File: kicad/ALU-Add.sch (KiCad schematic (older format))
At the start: 12 parts, among them U81 74LS245, U82 74LS283, U83 74LS283, U84 74LS86, U85 74LS86, U86 74LS86, U87 74LS86, U88 74LS86, U89 74LS86, U90 74LS86, U91 74LS86, U92 74LS86

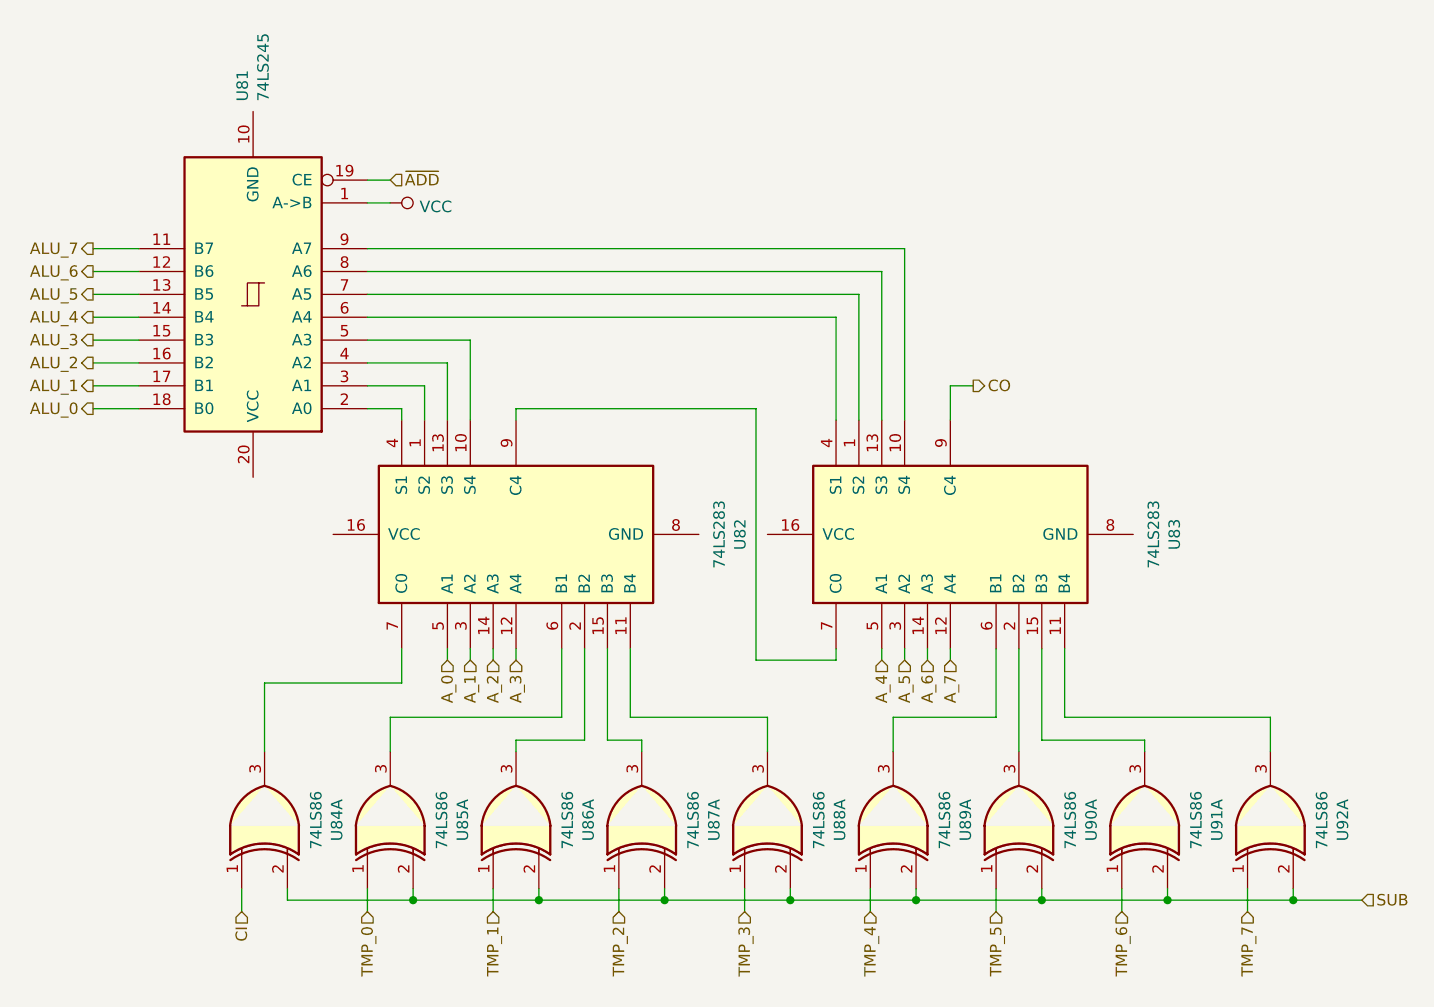
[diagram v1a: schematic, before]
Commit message: Reorganize part references
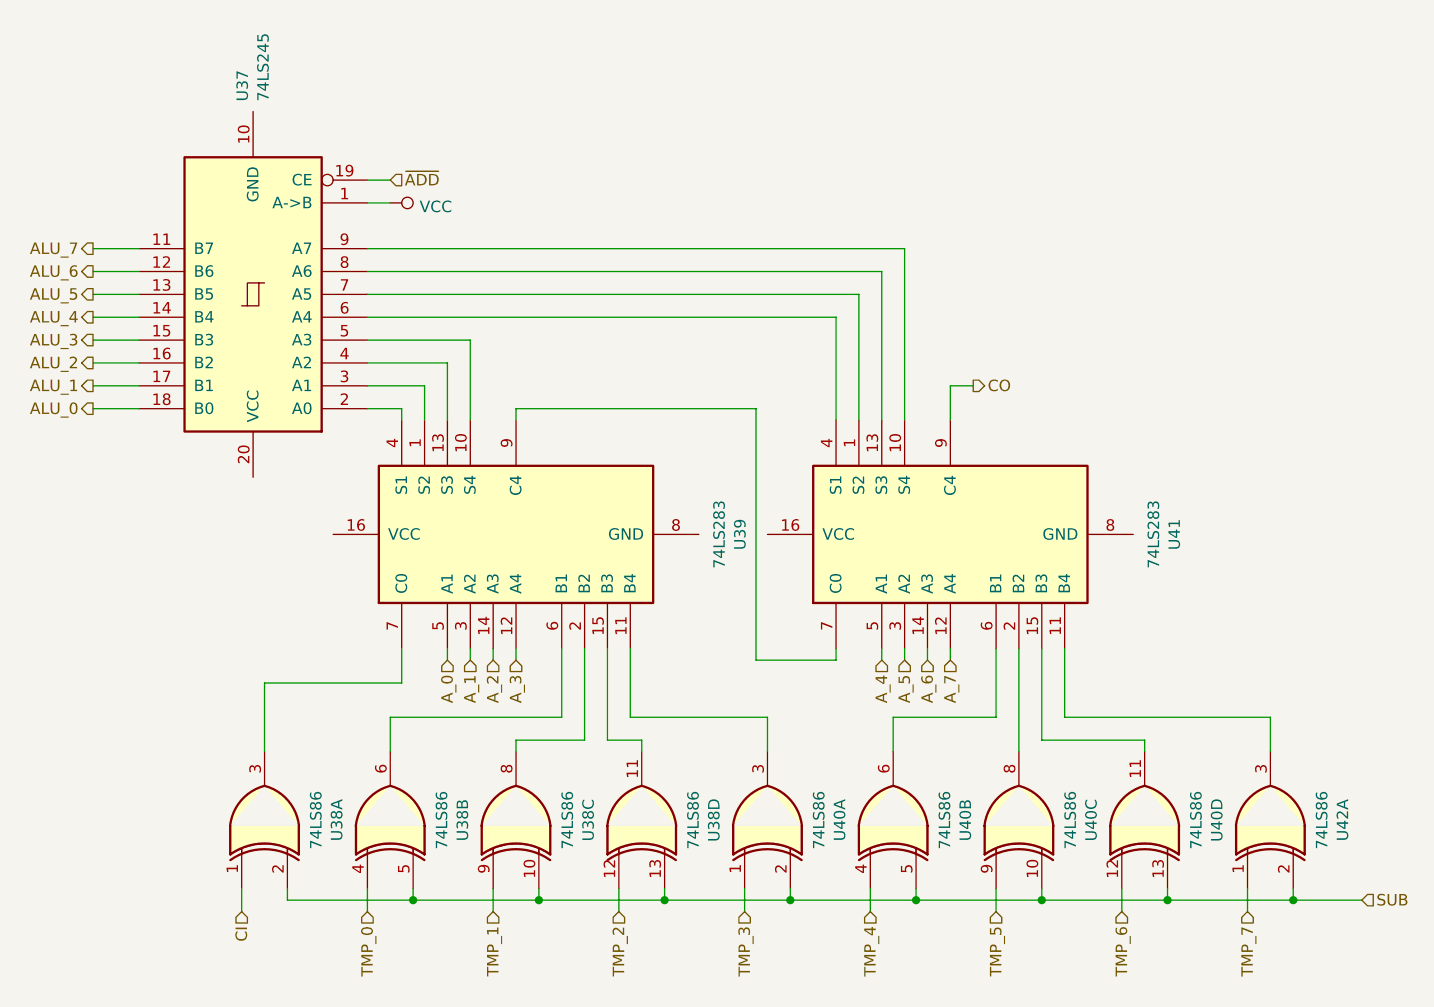
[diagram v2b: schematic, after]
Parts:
- renumbered U81 to U37, U84 to U38, U86 to U38, U85 to U38, U87 to U38, U82 to U39, U88 to U40, U90 to U40, U89 to U40, U91 to U40, U83 to U41, U92 to U42
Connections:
- net SUB: now also U38.10, U38.13, U38.5, U40.10, U40.13, U40.5; no longer U38.2, U38.2, U38.2, U40.2, U40.2, U40.2
- net TMP_0: now also U38.4; no longer U38.1
- net TMP_1: now also U38.9; no longer U38.1
- net TMP_2: now also U38.12; no longer U38.1
- net TMP_4: now also U40.4; no longer U40.1
- net TMP_5: now also U40.9; no longer U40.1
- net TMP_6: now also U40.12; no longer U40.1
- net at U39.2 (B2): now also U38.8; no longer U38.3
- net at U39.6 (B1): now also U38.6; no longer U38.3
- net at U39.15 (B3): now also U38.11; no longer U38.3
- net at U41.2 (B2): now also U40.8; no longer U40.3
- net at U41.6 (B1): now also U40.6; no longer U40.3
- net at U41.15 (B3): now also U40.11; no longer U40.3
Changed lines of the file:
@@
 $Descr A4 11693 8268
 encoding utf-8
-Sheet 23 26
+Sheet 10 26
 Title ""
 Date "2019-10-03"
@@
 AR Path="/5E5B2E62/5D96F636" Ref="U?"  Part="1"
 AR Path="/5E5B2E62/5E0141CE/5D96F636" Ref="U?"  Part="1"
-AR Path="/5E5B2E62/5E0141CE/5D94D587/5D96F636" Ref="U84"  Part="1"
-F 0 "U84" H 3200 4933 50  0000 C CNN
+AR Path="/5E5B2E62/5E0141CE/5D94D587/5D96F636" Ref="U38"  Part="1"
+F 0 "U38" H 3200 4933 50  0000 C CNN
 F 1 "74LS86" H 3200 5024 50  0000 C CNN
 F 2 "" H 3200 5250 50  0001 C CNN
@@
 $Comp
 L 74xx:74LS86 U?
-U 1 1 5D96F66E
+U 3 1 5D96F66E
 P 4300 5250
 AR Path="/5E5B2E62/5D96F66E" Ref="U?"  Part="1"
 AR Path="/5E5B2E62/5E0141CE/5D96F66E" Ref="U?"  Part="1"
-AR Path="/5E5B2E62/5E0141CE/5D94D587/5D96F66E" Ref="U86"  Part="1"
-F 0 "U86" H 4300 4933 50  0000 C CNN
+AR Path="/5E5B2E62/5E0141CE/5D94D587/5D96F66E" Ref="U38"  Part="3"
+F 0 "U38" H 4300 4933 50  0000 C CNN
 F 1 "74LS86" H 4300 5024 50  0000 C CNN
 F 2 "" H 4300 5250 50  0001 C CNN
 F 3 "74xx/74ls86.pdf" H 4300 5250 50  0001 C CNN
-	1    4300 5250
-	0    -1   -1   0
-$EndComp
-$Comp
-L 74xx:74LS86 U?
-U 1 1 5D96F674
+	3    4300 5250
+	0    -1   -1   0
+$EndComp
+$Comp
+L 74xx:74LS86 U?
+U 2 1 5D96F674
 P 3750 5250
 AR Path="/5E5B2E62/5D96F674" Ref="U?"  Part="1"
 AR Path="/5E5B2E62/5E0141CE/5D96F674" Ref="U?"  Part="1"
-AR Path="/5E5B2E62/5E0141CE/5D94D587/5D96F674" Ref="U85"  Part="1"
-F 0 "U85" H 3750 4933 50  0000 C CNN
+AR Path="/5E5B2E62/5E0141CE/5D94D587/5D96F674" Ref="U38"  Part="2"
+F 0 "U38" H 3750 4933 50  0000 C CNN
 F 1 "74LS86" H 3750 5024 50  0000 C CNN
 F 2 "" H 3750 5250 50  0001 C CNN
 F 3 "74xx/74ls86.pdf" H 3750 5250 50  0001 C CNN
-	1    3750 5250
+	2    3750 5250
 	0    -1   -1   0
 $EndComp
@@
 AR Path="/5E5B2E62/5D96F67A" Ref="U?"  Part="1"
 AR Path="/5E5B2E62/5E0141CE/5D96F67A" Ref="U?"  Part="1"
-AR Path="/5E5B2E62/5E0141CE/5D94D587/5D96F67A" Ref="U88"  Part="1"
-F 0 "U88" H 5400 4933 50  0000 C CNN
+AR Path="/5E5B2E62/5E0141CE/5D94D587/5D96F67A" Ref="U40"  Part="1"
+F 0 "U40" H 5400 4933 50  0000 C CNN
 F 1 "74LS86" H 5400 5024 50  0000 C CNN
 F 2 "" H 5400 5250 50  0001 C CNN
@@
 $Comp
 L 74xx:74LS86 U?
-U 1 1 5D96F680
+U 4 1 5D96F680
 P 4850 5250
 AR Path="/5E5B2E62/5D96F680" Ref="U?"  Part="1"
 AR Path="/5E5B2E62/5E0141CE/5D96F680" Ref="U?"  Part="1"
-AR Path="/5E5B2E62/5E0141CE/5D94D587/5D96F680" Ref="U87"  Part="1"
-F 0 "U87" H 4850 4933 50  0000 C CNN
+AR Path="/5E5B2E62/5E0141CE/5D94D587/5D96F680" Ref="U38"  Part="4"
+F 0 "U38" H 4850 4933 50  0000 C CNN
 F 1 "74LS86" H 4850 5024 50  0000 C CNN
 F 2 "" H 4850 5250 50  0001 C CNN
 F 3 "74xx/74ls86.pdf" H 4850 5250 50  0001 C CNN
-	1    4850 5250
+	4    4850 5250
 	0    -1   -1   0
 $EndComp
@@
 $Comp
 L 74xx:74LS86 U?
-U 1 1 5D96F68F
+U 3 1 5D96F68F
 P 6500 5250
 AR Path="/5E5B2E62/5D96F68F" Ref="U?"  Part="1"
 AR Path="/5E5B2E62/5E0141CE/5D96F68F" Ref="U?"  Part="1"
-AR Path="/5E5B2E62/5E0141CE/5D94D587/5D96F68F" Ref="U90"  Part="1"
-F 0 "U90" H 6500 4933 50  0000 C CNN
+AR Path="/5E5B2E62/5E0141CE/5D94D587/5D96F68F" Ref="U40"  Part="3"
+F 0 "U40" H 6500 4933 50  0000 C CNN
 F 1 "74LS86" H 6500 5024 50  0000 C CNN
 F 2 "" H 6500 5250 50  0001 C CNN
 F 3 "74xx/74ls86.pdf" H 6500 5250 50  0001 C CNN
-	1    6500 5250
-	0    -1   -1   0
-$EndComp
-$Comp
-L 74xx:74LS86 U?
-U 1 1 5D96F695
+	3    6500 5250
+	0    -1   -1   0
+$EndComp
+$Comp
+L 74xx:74LS86 U?
+U 2 1 5D96F695
 P 5950 5250
 AR Path="/5E5B2E62/5D96F695" Ref="U?"  Part="1"
 AR Path="/5E5B2E62/5E0141CE/5D96F695" Ref="U?"  Part="1"
-AR Path="/5E5B2E62/5E0141CE/5D94D587/5D96F695" Ref="U89"  Part="1"
-F 0 "U89" H 5950 4933 50  0000 C CNN
+AR Path="/5E5B2E62/5E0141CE/5D94D587/5D96F695" Ref="U40"  Part="2"
+F 0 "U40" H 5950 4933 50  0000 C CNN
 F 1 "74LS86" H 5950 5024 50  0000 C CNN
 F 2 "" H 5950 5250 50  0001 C CNN
 F 3 "74xx/74ls86.pdf" H 5950 5250 50  0001 C CNN
-	1    5950 5250
+	2    5950 5250
 	0    -1   -1   0
 $EndComp
@@
 AR Path="/5E5B2E62/5D96F69B" Ref="U?"  Part="1"
 AR Path="/5E5B2E62/5E0141CE/5D96F69B" Ref="U?"  Part="1"
-AR Path="/5E5B2E62/5E0141CE/5D94D587/5D96F69B" Ref="U92"  Part="1"
-F 0 "U92" H 7600 4933 50  0000 C CNN
+AR Path="/5E5B2E62/5E0141CE/5D94D587/5D96F69B" Ref="U42"  Part="1"
+F 0 "U42" H 7600 4933 50  0000 C CNN
 F 1 "74LS86" H 7600 5024 50  0000 C CNN
 F 2 "" H 7600 5250 50  0001 C CNN
@@
 $Comp
 L 74xx:74LS86 U?
-U 1 1 5D96F6A1
+U 4 1 5D96F6A1
 P 7050 5250
 AR Path="/5E5B2E62/5D96F6A1" Ref="U?"  Part="1"
 AR Path="/5E5B2E62/5E0141CE/5D96F6A1" Ref="U?"  Part="1"
-AR Path="/5E5B2E62/5E0141CE/5D94D587/5D96F6A1" Ref="U91"  Part="1"
-F 0 "U91" H 7050 4933 50  0000 C CNN
+AR Path="/5E5B2E62/5E0141CE/5D94D587/5D96F6A1" Ref="U40"  Part="4"
+F 0 "U40" H 7050 4933 50  0000 C CNN
 F 1 "74LS86" H 7050 5024 50  0000 C CNN
 F 2 "" H 7050 5250 50  0001 C CNN
 F 3 "74xx/74ls86.pdf" H 7050 5250 50  0001 C CNN
-	1    7050 5250
+	4    7050 5250
 	0    -1   -1   0
 $EndComp
@@
 AR Path="/5E5B2E62/5D96F6BB" Ref="U?"  Part="1"
 AR Path="/5E5B2E62/5E0141CE/5D96F6BB" Ref="U?"  Part="1"
-AR Path="/5E5B2E62/5E0141CE/5D94D587/5D96F6BB" Ref="U82"  Part="1"
-F 0 "U82" H 4300 3019 50  0000 C CNN
+AR Path="/5E5B2E62/5E0141CE/5D94D587/5D96F6BB" Ref="U39"  Part="1"
+F 0 "U39" H 4300 3019 50  0000 C CNN
 F 1 "74LS283" H 4300 3110 50  0000 C CNN
 F 2 "" H 4300 4000 50  0001 C CNN
@@
 AR Path="/5E5B2E62/5D96F6C1" Ref="U?"  Part="1"
 AR Path="/5E5B2E62/5E0141CE/5D96F6C1" Ref="U?"  Part="1"
-AR Path="/5E5B2E62/5E0141CE/5D94D587/5D96F6C1" Ref="U83"  Part="1"
-F 0 "U83" H 6200 3019 50  0000 C CNN
+AR Path="/5E5B2E62/5E0141CE/5D94D587/5D96F6C1" Ref="U41"  Part="1"
+F 0 "U41" H 6200 3019 50  0000 C CNN
 F 1 "74LS283" H 6200 3110 50  0000 C CNN
 F 2 "" H 6200 4000 50  0001 C CNN
@@
 P 3150 2950
 AR Path="/5E5B2E62/5E1111DF" Ref="U?"  Part="1"
-AR Path="/5E5B2E62/5E0141CE/5D94D587/5E1111DF" Ref="U81"  Part="1"
-F 0 "U81" V 3196 2106 50  0000 R CNN
+AR Path="/5E5B2E62/5E0141CE/5D94D587/5E1111DF" Ref="U37"  Part="1"
+F 0 "U37" V 3196 2106 50  0000 R CNN
 F 1 "74LS245" V 3105 2106 50  0000 R CNN
 F 2 "" H 3150 2950 50  0001 C CNN
